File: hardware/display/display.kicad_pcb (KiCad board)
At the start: 2 copper layers, 110 x 70 mm, 7 parts, among them J1 Conn_02x03_Odd_Even

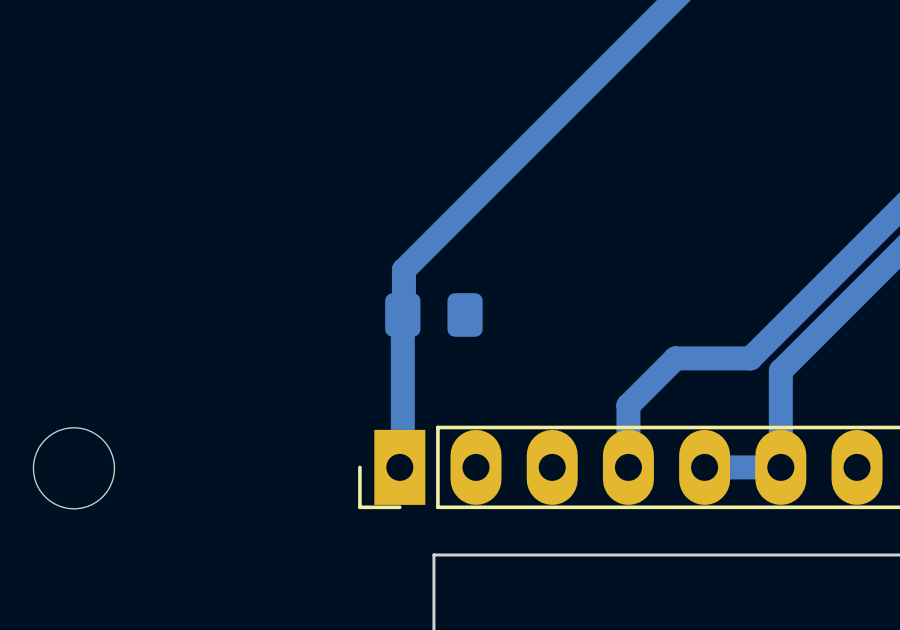
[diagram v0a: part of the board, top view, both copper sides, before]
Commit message: Adjust PCBs after reference and footprint changes
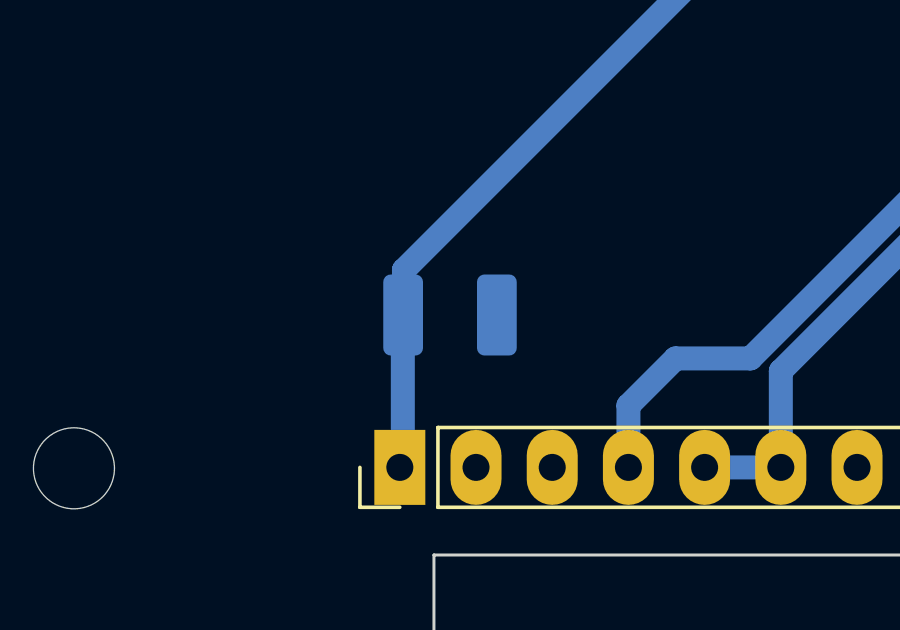
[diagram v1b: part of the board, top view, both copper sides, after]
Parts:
- C1: value 100nF -> 10µ; footprint Capacitor_SMD:C_0805_2012Metric_Pad1.18x1.45mm_HandSolder -> Capacitor_SMD:C_1210_3225Metric_Pad1.33x2.70mm_HandSolder
- moved C1 0.53 mm to (89.5, 128.0)
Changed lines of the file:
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@@
       (net 10 "/~{RST_DISP}") (pinfunction "Pin_6") (pintype "passive"))
   )
-  (footprint "Capacitor_SMD:C_0805_2012Metric_Pad1.18x1.45mm_HandSolder" (layer "B.Cu")
-    (at 89 128 180)
-    (descr "Capacitor SMD 0805 (2012 Metric), square (rectangular) end terminal, IPC_7351 nominal with elongated pad for handsoldering. (Body size source: IPC-SM-782 page 76, https://www.pcb-3d.com/wordpress/wp-content/uploads/ipc-sm-782a_amendment_1_and_2.pdf, https://docs.google.com/spreadsheets/d/1BsfQQcO9C6DZCsRaXUlFlo91Tg2WpOkGARC1WS5S8t0/edit?usp=sharing), generated with kicad-footprint-generator")
+  (footprint "Capacitor_SMD:C_1210_3225Metric_Pad1.33x2.70mm_HandSolder" (layer "B.Cu")
+    (at 89.535 128 180)
+    (descr "Capacitor SMD 1210 (3225 Metric), square (rectangular) end terminal, IPC_7351 nominal with elongated pad for handsoldering. (Body size source: IPC-SM-782 page 76, https://www.pcb-3d.com/wordpress/wp-content/uploads/ipc-sm-782a_amendment_1_and_2.pdf), generated with kicad-footprint-generator")
     (tags "capacitor handsolder")
+    (property "P/N" "C3225X5R1E106K250AA (stock)")
     (property "Sheetfile" "display.kicad_sch")
     (property "Sheetname" "")
     (attr smd)
-    (fp_text reference "C1" (at 0 1.68) (layer "B.SilkS")
+    (fp_text reference "C1" (at 0 2.3) (layer "B.SilkS")
       (effects (font (size 1 1) (thickness 0.15)) (justify mirror))
     )
-    (fp_text value "100nF" (at 0 -1.68) (layer "B.Fab")
+    (fp_text value "10µ" (at 0 -2.3) (layer "B.Fab")
       (effects (font (size 1 1) (thickness 0.15)) (justify mirror))
     )
     (fp_text user "${REFERENCE}" (at 0 0) (layer "B.Fab")
-      (effects (font (size 0.5 0.5) (thickness 0.08)) (justify mirror))
+      (effects (font (size 0.8 0.8) (thickness 0.12)) (justify mirror))
     )
-    (fp_line (start -0.261252 -0.735) (end 0.261252 -0.735) (layer "B.SilkS") (width 0.12))
-    (fp_line (start -0.261252 0.735) (end 0.261252 0.735) (layer "B.SilkS") (width 0.12))
-    (fp_line (start -1.88 -0.98) (end -1.88 0.98) (layer "B.CrtYd") (width 0.05))
-    (fp_line (start 1.88 0.98) (end 1.88 -0.98) (layer "B.CrtYd") (width 0.05))
-    (fp_line (start 1.88 -0.98) (end -1.88 -0.98) (layer "B.CrtYd") (width 0.05))
-    (fp_line (start -1.88 0.98) (end 1.88 0.98) (layer "B.CrtYd") (width 0.05))
-    (fp_line (start 1 0.625) (end 1 -0.625) (layer "B.Fab") (width 0.1))
-    (fp_line (start 1 -0.625) (end -1 -0.625) (layer "B.Fab") (width 0.1))
-    (fp_line (start -1 -0.625) (end -1 0.625) (layer "B.Fab") (width 0.1))
-    (fp_line (start -1 0.625) (end 1 0.625) (layer "B.Fab") (width 0.1))
-    (pad "1" smd roundrect (at -1.0375 0 180) (size 1.175 1.45) (layers "B.Cu" "B.Paste" "B.Mask") (roundrect_rratio 0.212766)
+    (fp_line (start -0.711252 -1.36) (end 0.711252 -1.36) (layer "B.SilkS") (width 0.12))
+    (fp_line (start -0.711252 1.36) (end 0.711252 1.36) (layer "B.SilkS") (width 0.12))
+    (fp_line (start 2.48 1.6) (end 2.48 -1.6) (layer "B.CrtYd") (width 0.05))
+    (fp_line (start 2.48 -1.6) (end -2.48 -1.6) (layer "B.CrtYd") (width 0.05))
+    (fp_line (start -2.48 -1.6) (end -2.48 1.6) (layer "B.CrtYd") (width 0.05))
+    (fp_line (start -2.48 1.6) (end 2.48 1.6) (layer "B.CrtYd") (width 0.05))
+    (fp_line (start -1.6 1.25) (end 1.6 1.25) (layer "B.Fab") (width 0.1))
+    (fp_line (start 1.6 -1.25) (end -1.6 -1.25) (layer "B.Fab") (width 0.1))
+    (fp_line (start 1.6 1.25) (end 1.6 -1.25) (layer "B.Fab") (width 0.1))
+    (fp_line (start -1.6 -1.25) (end -1.6 1.25) (layer "B.Fab") (width 0.1))
+    (pad "1" smd roundrect (at -1.5625 0 180) (size 1.325 2.7) (layers "B.Cu" "B.Paste" "B.Mask") (roundrect_rratio 0.188679)
       (net 1 "GND") (pintype "passive"))
-    (pad "2" smd roundrect (at 1.0375 0 180) (size 1.175 1.45) (layers "B.Cu" "B.Paste" "B.Mask") (roundrect_rratio 0.212766)
+    (pad "2" smd roundrect (at 1.5625 0 180) (size 1.325 2.7) (layers "B.Cu" "B.Paste" "B.Mask") (roundrect_rratio 0.188679)
       (net 2 "+5V") (pintype "passive"))
-    (model "${KICAD6_3DMODEL_DIR}/Capacitor_SMD.3dshapes/C_0805_2012Metric.wrl"
+    (model "${KICAD6_3DMODEL_DIR}/Capacitor_SMD.3dshapes/C_1210_3225Metric.wrl"
       (offset (xyz 0 0 0))
       (scale (xyz 1 1 1))

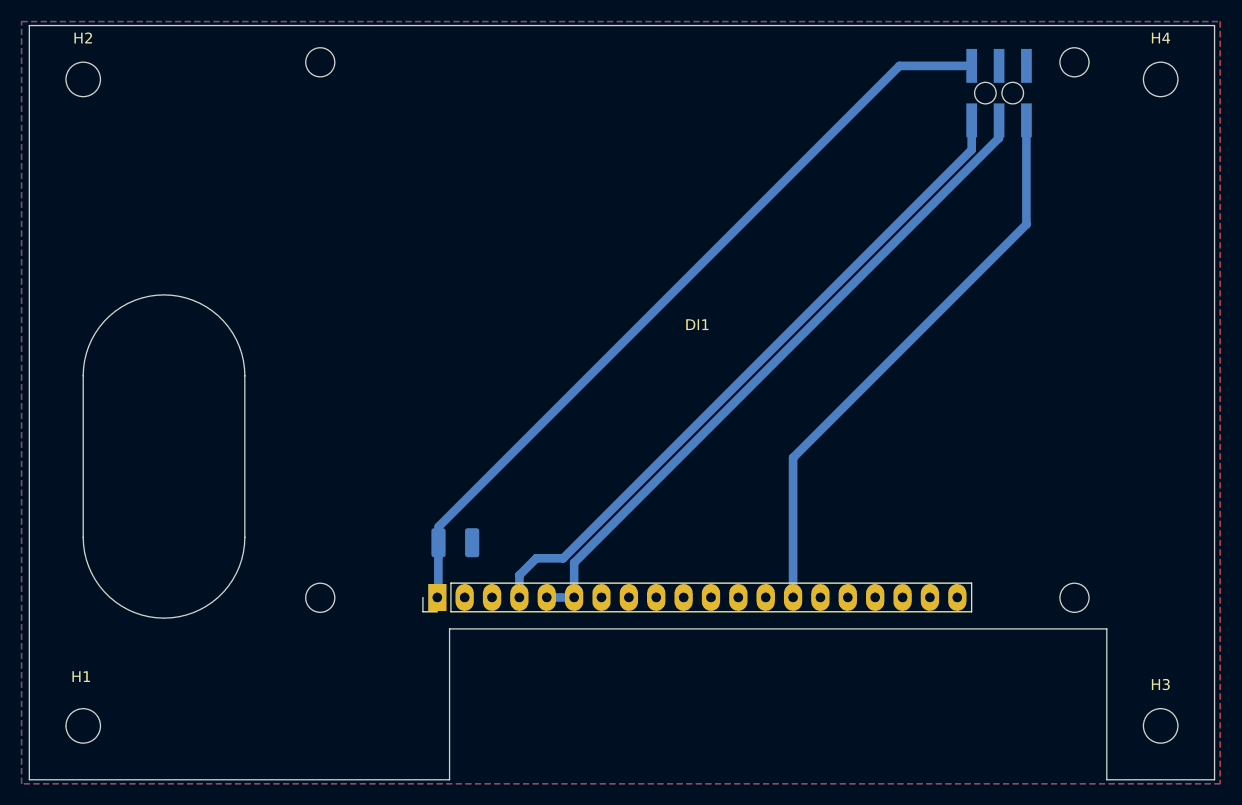
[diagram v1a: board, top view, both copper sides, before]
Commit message: Adjust for "0 height" display nuts
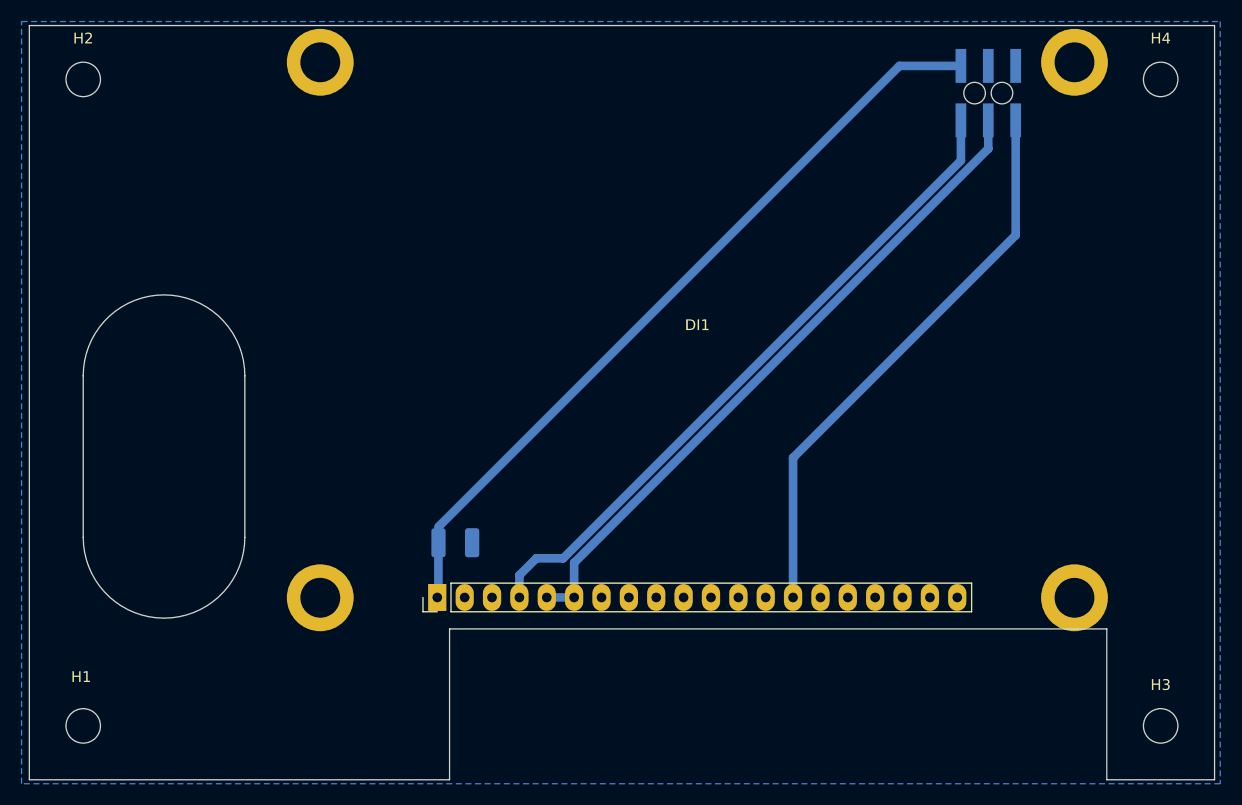
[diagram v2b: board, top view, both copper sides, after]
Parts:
- moved J1 1.00 mm to (139.0, 86.3)
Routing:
- net +5V: track 73.6 -> 72.6 mm
- removed copper zone on F.Cu, net GND
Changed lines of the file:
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@@
     (fp_circle (center 34.59 -20.54) (end 34.59 -20.54) (layer "User.9") (width 0.12) (fill none))
     (fp_circle (center -35.41 29.16) (end -35.41 29.16) (layer "User.9") (width 0.12) (fill none))
-    (pad "" np_thru_hole circle (at 35 -21.59) (size 2.7 2.7) (drill 2.7) (layers F&B.Cu *.Mask))
-    (pad "" np_thru_hole circle (at -35 -21.59) (size 2.7 2.7) (drill 2.7) (layers F&B.Cu *.Mask))
-    (pad "" np_thru_hole circle (at -35 28.11) (size 2.7 2.7) (drill 2.7) (layers F&B.Cu *.Mask))
-    (pad "" np_thru_hole circle (at 35 28.11) (size 2.7 2.7) (drill 2.7) (layers F&B.Cu *.Mask))
+    (pad "" thru_hole circle (at 35 -21.59) (size 6.2 6.2) (drill 3.7) (layers *.Cu *.Mask))
+    (pad "" thru_hole circle (at -35 -21.59) (size 6.2 6.2) (drill 3.7) (layers *.Cu *.Mask))
+    (pad "" thru_hole circle (at -35 28.11) (size 6.2 6.2) (drill 3.7) (layers *.Cu *.Mask))
+    (pad "" thru_hole circle (at 35 28.11) (size 6.2 6.2) (drill 3.7) (layers *.Cu *.Mask))
     (pad "1" thru_hole rect (at -24.1375 28.08 90) (size 2.5 1.7) (drill 0.9) (layers *.Cu *.Mask)
       (net 2 "+5V") (pinfunction "VDD") (pintype "power_in"))
@@
     (pad "" np_thru_hole circle locked (at 0 0) (size 3.2 3.2) (drill 3.2) (layers *.Cu *.Mask))
   )
-  (footprint "harwin:M20-8750342" (layer "B.Cu")
-    (at 140 86.27 -90)
+  (footprint "harwin:M20-8750342" locked (layer "B.Cu")
+    (at 139 86.27 -90)
     (property "P/N" " M20-8750342 ")
     (property "Sheetfile" "display.kicad_sch")
@@
     (fp_line (start 3.6 0.32) (end 3.6 -0.32) (layer "B.Fab") (width 0.1))
     (fp_line (start 2.54 2.86) (end 3.6 2.86) (layer "B.Fab") (width 0.1))
-    (pad "" np_thru_hole circle (at 0 1.27 270) (size 2 2) (drill 2) (layers F&B.Cu *.Mask))
-    (pad "" np_thru_hole circle (at 0 -1.27 270) (size 2 2) (drill 2) (layers F&B.Cu *.Mask))
-    (pad "1" smd rect (at -2.525 2.54 270) (size 3.15 1) (layers "B.Cu" "B.Paste" "B.Mask")
+    (pad "" np_thru_hole circle locked (at 0 1.27 270) (size 2 2) (drill 2) (layers F&B.Cu *.Mask))
+    (pad "" np_thru_hole circle locked (at 0 -1.27 270) (size 2 2) (drill 2) (layers F&B.Cu *.Mask))
+    (pad "1" smd rect locked (at -2.525 2.54 270) (size 3.15 1) (layers "B.Cu" "B.Paste" "B.Mask")
       (net 2 "+5V") (pinfunction "Pin_1") (pintype "passive"))
-    (pad "2" smd rect (at -2.525 0 270) (size 3.15 1) (layers "B.Cu" "B.Paste" "B.Mask")
+    (pad "2" smd rect locked (at -2.525 0 270) (size 3.15 1) (layers "B.Cu" "B.Paste" "B.Mask")
       (net 11 "unconnected-(J1-Pad2)") (pinfunction "Pin_2") (pintype "passive+no_connect"))
-    (pad "3" smd rect (at -2.525 -2.54 270) (size 3.15 1) (layers "B.Cu" "B.Paste" "B.Mask")
+    (pad "3" smd rect locked (at -2.525 -2.54 270) (size 3.15 1) (layers "B.Cu" "B.Paste" "B.Mask")
       (net 1 "GND") (pinfunction "Pin_3") (pintype "passive"))
-    (pad "4" smd rect (at 2.525 2.54 270) (size 3.15 1) (layers "B.Cu" "B.Paste" "B.Mask")
+    (pad "4" smd rect locked (at 2.525 2.54 270) (size 3.15 1) (layers "B.Cu" "B.Paste" "B.Mask")
       (net 8 "/SCL") (pinfunction "Pin_4") (pintype "passive"))
-    (pad "5" smd rect (at 2.525 0 270) (size 3.15 1) (layers "B.Cu" "B.Paste" "B.Mask")
+    (pad "5" smd rect locked (at 2.525 0 270) (size 3.15 1) (layers "B.Cu" "B.Paste" "B.Mask")
       (net 9 "/SDA") (pinfunction "Pin_5") (pintype "passive"))
-    (pad "6" smd rect (at 2.525 -2.54 270) (size 3.15 1) (layers "B.Cu" "B.Paste" "B.Mask")
+    (pad "6" smd rect locked (at 2.525 -2.54 270) (size 3.15 1) (layers "B.Cu" "B.Paste" "B.Mask")
       (net 10 "/~{RST_DISP}") (pinfunction "Pin_6") (pintype "passive"))
   )
@@
   (segment (start 87.9625 128) (end 87.9625 132.98) (width 0.8) (layer "B.Cu") (net 2))
   (segment (start 130.755 83.745) (end 88 126.5) (width 0.8) (layer "B.Cu") (net 2))
+  (segment (start 136.46 83.745) (end 130.755 83.745) (width 0.8) (layer "B.Cu") (net 2))
   (segment (start 88 126.5) (end 88 127.9625) (width 0.8) (layer "B.Cu") (net 2))
-  (segment (start 137.46 83.745) (end 130.755 83.745) (width 0.8) (layer "B.Cu") (net 2))
-  (segment (start 137.46 88.795) (end 137.46 91.54) (width 0.8) (layer "B.Cu") (net 8))
-  (segment (start 99.5525 129.4475) (end 97.0525 129.4475) (width 0.8) (layer "B.Cu") (net 8))
   (segment (start 95.4825 131.0175) (end 95.4825 133.08) (width 0.8) (layer "B.Cu") (net 8))
   (segment (start 97.0525 129.4475) (end 95.4825 131.0175) (width 0.8) (layer "B.Cu") (net 8))
-  (segment (start 137.46 91.54) (end 99.5525 129.4475) (width 0.8) (layer "B.Cu") (net 8))
-  (segment (start 140 88.795) (end 140 90.428356) (width 0.8) (layer "B.Cu") (net 9))
+  (segment (start 136.46 88.795) (end 136.46 92.54) (width 0.8) (layer "B.Cu") (net 8))
+  (segment (start 136.46 92.54) (end 99.5525 129.4475) (width 0.8) (layer "B.Cu") (net 8))
+  (segment (start 99.5525 129.4475) (end 97.0525 129.4475) (width 0.8) (layer "B.Cu") (net 8))
+  (segment (start 139 91.428356) (end 100.5625 129.865856) (width 0.8) (layer "B.Cu") (net 9))
   (segment (start 100.5625 129.865856) (end 100.5625 133.08) (width 0.8) (layer "B.Cu") (net 9))
-  (segment (start 140 90.428356) (end 100.5625 129.865856) (width 0.8) (layer "B.Cu") (net 9))
+  (segment (start 139 88.795) (end 139 91.428356) (width 0.8) (layer "B.Cu") (net 9))
   (segment (start 98.0225 133.08) (end 100.5625 133.08) (width 0.8) (layer "B.Cu") (net 9))
-  (segment (start 142.54 98.46) (end 120.8825 120.1175) (width 0.8) (layer "B.Cu") (net 10))
+  (segment (start 141.54 99.46) (end 120.8825 120.1175) (width 0.8) (layer "B.Cu") (net 10))
   (segment (start 120.8825 120.1175) (end 120.8825 133.08) (width 0.8) (layer "B.Cu") (net 10))
-  (segment (start 142.54 88.795) (end 142.54 98.46) (width 0.8) (layer "B.Cu") (net 10))
-  (zone (net 1) (net_name "GND") (layers F&B.Cu) (hatch edge 0.508)
+  (segment (start 141.54 88.795) (end 141.54 99.46) (width 0.8) (layer "B.Cu") (net 10))
+  (zone (net 1) (net_name "GND") (layer "B.Cu") (hatch edge 0.508)
     (connect_pads (clearance 0.21))
     (min_thickness 0.254) (filled_areas_thickness no)
